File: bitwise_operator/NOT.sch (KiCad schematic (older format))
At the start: 3 parts, among them U13 74LS04, U14 74LS04, U15 74LS04

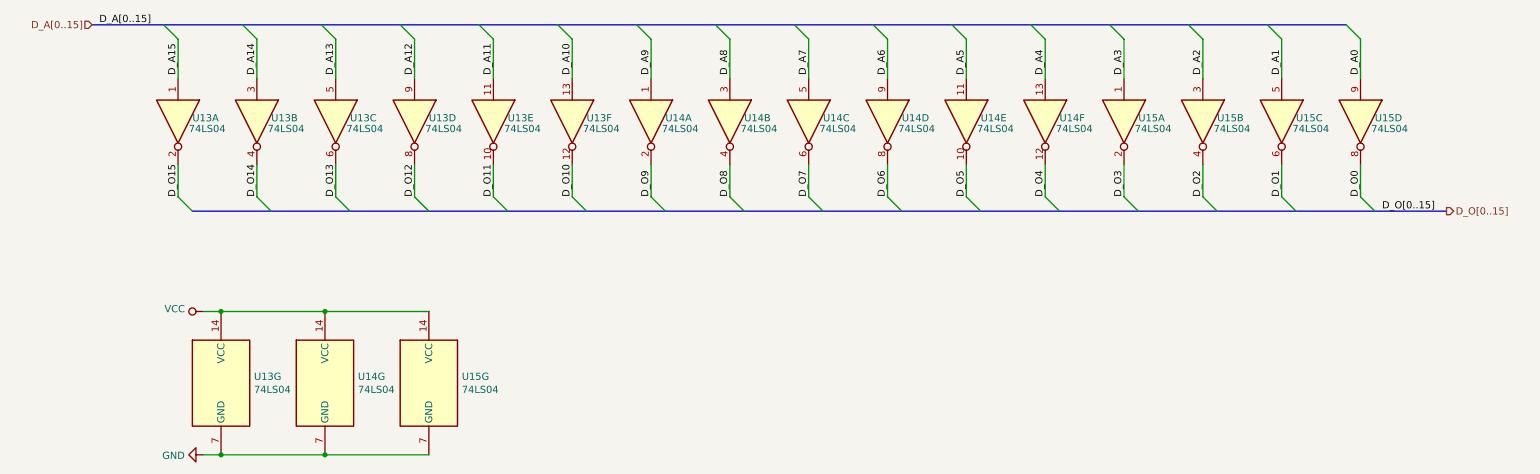
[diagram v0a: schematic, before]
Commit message: add bit operations
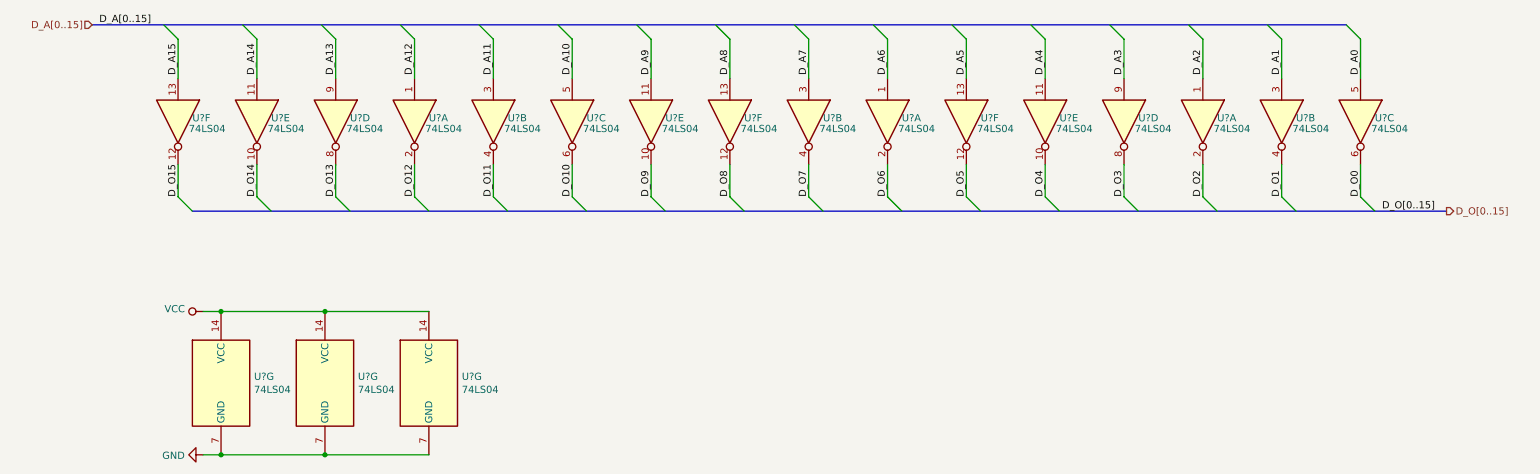
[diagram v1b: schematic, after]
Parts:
- renumbered U13 to U?, U14 to U?, U15 to U?
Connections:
- net D_A0: now also U?.5; no longer U?.9
- net D_A1: now also U?.3; no longer U?.5
- net D_A10: now also U?.5; no longer U?.13
- net D_A11: now also U?.3; no longer U?.11
- net D_A12: now also U?.1; no longer U?.9
- net D_A13: now also U?.9; no longer U?.5
- net D_A14: now also U?.11; no longer U?.3
- net D_A15: now also U?.13; no longer U?.1
- net D_A2: now also U?.1; no longer U?.3
- net D_A3: now also U?.9; no longer U?.1
- net D_A4: now also U?.11; no longer U?.13
- net D_A5: now also U?.13; no longer U?.11
- net D_A6: now also U?.1; no longer U?.9
- net D_A7: now also U?.3; no longer U?.5
- net D_A8: now also U?.13; no longer U?.3
- net D_A9: now also U?.11; no longer U?.1
- net D_O0: now also U?.6; no longer U?.8
- net D_O1: now also U?.4; no longer U?.6
- net D_O10: now also U?.6; no longer U?.12
- net D_O11: now also U?.4; no longer U?.10
- net D_O12: now also U?.2; no longer U?.8
- net D_O13: now also U?.8; no longer U?.6
- net D_O14: now also U?.10; no longer U?.4
- net D_O15: now also U?.12; no longer U?.2
- net D_O2: now also U?.2; no longer U?.4
- net D_O3: now also U?.8; no longer U?.2
- net D_O4: now also U?.10; no longer U?.12
- net D_O5: now also U?.12; no longer U?.10
- net D_O6: now also U?.2; no longer U?.8
- net D_O7: now also U?.4; no longer U?.6
- net D_O8: now also U?.12; no longer U?.4
- net D_O9: now also U?.10; no longer U?.2

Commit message: part lists
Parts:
- gave numbers to parts that had none: 3
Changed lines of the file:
@@
 EESchema Schematic File Version 4
-LIBS:computer-cache
+LIBS:bitwise_operator_pcb-cache
 EELAYER 30 0
 EELAYER END
 $Descr A4 11693 8268
 encoding utf-8
-Sheet 6 36
+Sheet 6 13
 Title ""
 Date ""
@@
 AR Path="/5F0D7DA0/5F3B3AEB/5F302CCB" Ref="#PWR?"  Part="1"
 AR Path="/5F0D7DA0/5F3EC2E5/5F302CCB" Ref="#PWR0109"  Part="1"
-F 0 "#PWR?" H 1950 4100 50  0001 C CNN
+F 0 "#PWR0109" H 1950 4100 50  0001 C CNN
 F 1 "VCC" V 1968 4377 50  0000 L CNN
 F 2 "" H 1950 4250 50  0001 C CNN
@@
 AR Path="/5F0D7DA0/5F3B3AEB/5F64958C" Ref="#PWR?"  Part="1"
 AR Path="/5F0D7DA0/5F3EC2E5/5F64958C" Ref="#PWR0110"  Part="1"
-F 0 "#PWR?" H 1950 5000 50  0001 C CNN
+F 0 "#PWR0110" H 1950 5000 50  0001 C CNN
 F 1 "GND" V 1955 5122 50  0000 R CNN
 F 2 "" H 1950 5250 50  0001 C CNN
@@
 D_O[0..15]
 $Comp
-L 74xx:74LS04 U?
+L 74xx:74LS04 U14
 U 5 1 5F410599
 P 5075 2925
-F 0 "U?" V 5050 3025 50  0000 L CNN
+F 0 "U14" V 5050 3025 50  0000 L CNN
 F 1 "74LS04" V 5125 3000 50  0000 L CNN
 F 2 "Package_DIP:DIP-14_W7.62mm_LongPads" H 5075 2925 50  0001 C CNN
@@
 $EndComp
 $Comp
-L 74xx:74LS04 U?
+L 74xx:74LS04 U14
 U 6 1 5F41059F
 P 5625 2925
-F 0 "U?" V 5600 3025 50  0000 L CNN
+F 0 "U14" V 5600 3025 50  0000 L CNN
 F 1 "74LS04" V 5675 3000 50  0000 L CNN
 F 2 "Package_DIP:DIP-14_W7.62mm_LongPads" H 5625 2925 50  0001 C CNN
@@
 $EndComp
 $Comp
-L 74xx:74LS04 U?
+L 74xx:74LS04 U14
 U 2 1 5F4105A5
 P 6175 2925
-F 0 "U?" V 6150 3025 50  0000 L CNN
+F 0 "U14" V 6150 3025 50  0000 L CNN
 F 1 "74LS04" V 6225 3000 50  0000 L CNN
 F 2 "Package_DIP:DIP-14_W7.62mm_LongPads" H 6175 2925 50  0001 C CNN
@@
 $EndComp
 $Comp
-L 74xx:74LS04 U?
+L 74xx:74LS04 U14
 U 1 1 5F4105AB
 P 6725 2925
-F 0 "U?" V 6700 3025 50  0000 L CNN
+F 0 "U14" V 6700 3025 50  0000 L CNN
 F 1 "74LS04" V 6775 3000 50  0000 L CNN
 F 2 "Package_DIP:DIP-14_W7.62mm_LongPads" H 6725 2925 50  0001 C CNN
@@
 $EndComp
 $Comp
-L 74xx:74LS04 U?
+L 74xx:74LS04 U15
 U 6 1 5F4105B1
 P 7275 2925
-F 0 "U?" V 7250 3025 50  0000 L CNN
+F 0 "U15" V 7250 3025 50  0000 L CNN
 F 1 "74LS04" V 7325 3000 50  0000 L CNN
 F 2 "Package_DIP:DIP-14_W7.62mm_LongPads" H 7275 2925 50  0001 C CNN
@@
 $EndComp
 $Comp
-L 74xx:74LS04 U?
+L 74xx:74LS04 U15
 U 5 1 5F4105B7
 P 7825 2925
-F 0 "U?" V 7800 3025 50  0000 L CNN
+F 0 "U15" V 7800 3025 50  0000 L CNN
 F 1 "74LS04" V 7875 3000 50  0000 L CNN
 F 2 "Package_DIP:DIP-14_W7.62mm_LongPads" H 7825 2925 50  0001 C CNN
@@
 $EndComp
 $Comp
-L 74xx:74LS04 U?
+L 74xx:74LS04 U15
 U 4 1 5F41371E
 P 8375 2925
-F 0 "U?" V 8350 3025 50  0000 L CNN
+F 0 "U15" V 8350 3025 50  0000 L CNN
 F 1 "74LS04" V 8425 3000 50  0000 L CNN
 F 2 "Package_DIP:DIP-14_W7.62mm_LongPads" H 8375 2925 50  0001 C CNN
@@
 $EndComp
 $Comp
-L 74xx:74LS04 U?
+L 74xx:74LS04 U15
 U 1 1 5F413724
 P 8925 2925
-F 0 "U?" V 8900 3025 50  0000 L CNN
+F 0 "U15" V 8900 3025 50  0000 L CNN
 F 1 "74LS04" V 8975 3000 50  0000 L CNN
 F 2 "Package_DIP:DIP-14_W7.62mm_LongPads" H 8925 2925 50  0001 C CNN
@@
 $EndComp
 $Comp
-L 74xx:74LS04 U?
+L 74xx:74LS04 U15
 U 2 1 5F41372A
 P 9475 2925
-F 0 "U?" V 9450 3025 50  0000 L CNN
+F 0 "U15" V 9450 3025 50  0000 L CNN
 F 1 "74LS04" V 9525 3000 50  0000 L CNN
 F 2 "Package_DIP:DIP-14_W7.62mm_LongPads" H 9475 2925 50  0001 C CNN
@@
 $EndComp
 $Comp
-L 74xx:74LS04 U?
+L 74xx:74LS04 U15
 U 3 1 5F413730
 P 10025 2925
-F 0 "U?" V 10000 3025 50  0000 L CNN
+F 0 "U15" V 10000 3025 50  0000 L CNN
 F 1 "74LS04" V 10075 3000 50  0000 L CNN
 F 2 "Package_DIP:DIP-14_W7.62mm_LongPads" H 10025 2925 50  0001 C CNN
@@
 	2075 5250 2800 5250
 $Comp
-L 74xx:74LS04 U?
+L 74xx:74LS04 U14
 U 7 1 5F4164D6
 P 2800 4750
-F 0 "U?" H 3030 4796 50  0000 L CNN
+F 0 "U14" H 3030 4796 50  0000 L CNN
 F 1 "74LS04" H 3030 4705 50  0000 L CNN
 F 2 "Package_DIP:DIP-14_W7.62mm_LongPads" H 2800 4750 50  0001 C CNN
@@
 	2800 5250 3525 5250
 $Comp
-L 74xx:74LS04 U?
+L 74xx:74LS04 U15
 U 7 1 5F41717A
 P 3525 4750
-F 0 "U?" H 3755 4796 50  0000 L CNN
+F 0 "U15" H 3755 4796 50  0000 L CNN
 F 1 "74LS04" H 3755 4705 50  0000 L CNN
 F 2 "Package_DIP:DIP-14_W7.62mm_LongPads" H 3525 4750 50  0001 C CNN
@@
 Text Label 1225 2250 0    50   ~ 0
 D_A[0..15]
-Wire Bus Line
-	1875 3550 10625 3550
-Wire Bus Line
-	1175 2250 9925 2250
-$Comp
-L 74xx:74LS04 U?
+$Comp
+L 74xx:74LS04 U13
 U 5 1 5F400D4F
 P 2325 2925
-F 0 "U?" V 2300 3025 50  0000 L CNN
+F 0 "U13" V 2300 3025 50  0000 L CNN
 F 1 "74LS04" V 2375 3000 50  0000 L CNN
 F 2 "Package_DIP:DIP-14_W7.62mm_LongPads" H 2325 2925 50  0001 C CNN
@@
 $EndComp
 $Comp
-L 74xx:74LS04 U?
+L 74xx:74LS04 U13
 U 7 1 5F41519D
 P 2075 4750
-F 0 "U?" H 2305 4796 50  0000 L CNN
+F 0 "U13" H 2305 4796 50  0000 L CNN
 F 1 "74LS04" H 2305 4705 50  0000 L CNN
 F 2 "Package_DIP:DIP-14_W7.62mm_LongPads" H 2075 4750 50  0001 C CNN
@@
 $EndComp
 $Comp
-L 74xx:74LS04 U?
+L 74xx:74LS04 U13
 U 3 1 5F4062E5
 P 4525 2925
-F 0 "U?" V 4500 3025 50  0000 L CNN
+F 0 "U13" V 4500 3025 50  0000 L CNN
 F 1 "74LS04" V 4575 3000 50  0000 L CNN
 F 2 "Package_DIP:DIP-14_W7.62mm_LongPads" H 4525 2925 50  0001 C CNN
@@
 $EndComp
 $Comp
-L 74xx:74LS04 U?
+L 74xx:74LS04 U13
 U 2 1 5F40519A
 P 3975 2925
-F 0 "U?" V 3950 3025 50  0000 L CNN
+F 0 "U13" V 3950 3025 50  0000 L CNN
 F 1 "74LS04" V 4025 3000 50  0000 L CNN
 F 2 "Package_DIP:DIP-14_W7.62mm_LongPads" H 3975 2925 50  0001 C CNN
@@
 $EndComp
 $Comp
-L 74xx:74LS04 U?
+L 74xx:74LS04 U13
 U 1 1 5F403E69
 P 3425 2925
-F 0 "U?" V 3400 3025 50  0000 L CNN
+F 0 "U13" V 3400 3025 50  0000 L CNN
 F 1 "74LS04" V 3475 3000 50  0000 L CNN
 F 2 "Package_DIP:DIP-14_W7.62mm_LongPads" H 3425 2925 50  0001 C CNN
@@
 $EndComp
 $Comp
-L 74xx:74LS04 U?
+L 74xx:74LS04 U13
 U 4 1 5F4022E2
 P 2875 2925
-F 0 "U?" V 2850 3025 50  0000 L CNN
+F 0 "U13" V 2850 3025 50  0000 L CNN
 F 1 "74LS04" V 2925 3000 50  0000 L CNN
 F 2 "Package_DIP:DIP-14_W7.62mm_LongPads" H 2875 2925 50  0001 C CNN
@@
 $EndComp
 $Comp
-L 74xx:74LS04 U?
+L 74xx:74LS04 U13
 U 6 1 5F3EED48
 P 1775 2925
-F 0 "U?" V 1750 3025 50  0000 L CNN
+F 0 "U13" V 1750 3025 50  0000 L CNN
 F 1 "74LS04" V 1825 3000 50  0000 L CNN
 F 2 "Package_DIP:DIP-14_W7.62mm_LongPads" H 1775 2925 50  0001 C CNN
@@
 	0    1    1    0
 $EndComp
+Wire Bus Line
+	1875 3550 10625 3550
+Wire Bus Line
+	1175 2250 9925 2250
 $EndSCHEMATC
